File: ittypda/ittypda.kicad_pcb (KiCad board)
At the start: 2 copper layers, 105 x 109.8 mm, 172 parts, among them CN1 S2B-PH-SM4-TB, J1 USB_C_Receptacle_USB2.0_14P, J13 Conn_01x05_Pin, J14 Conn_01x05_Pin, J2 Conn_01x04_Pin, SW1 Switch, SW10 Switch, SW11 Switch, SW12 Switch, SW13 Switch, SW14 Switch, SW15 Switch, SW16 Switch, SW17 Switch, SW18 Switch, SW19 Switch, SW2 Switch, SW20 Switch, SW21 Switch, SW22 Switch, SW23 Switch, SW24 Switch, SW25 SLIDE SWITCH, SW26 Switch, SW27 Switch, SW28 Switch, SW29 Switch, SW3 Switch, SW30 Switch, SW31 Switch, SW32 Switch, SW33 Switch, SW34 Switch, SW36 Switch, SW37 Switch, SW38 Switch, SW39 Switch, SW4 Switch, SW41 Switch, SW42 Switch, SW43 Switch, SW44 Switch, SW45 Switch, SW46 Switch, SW47 Switch, SW48 Switch, SW49 Switch, SW5 Switch, SW50 Switch, SW51 Switch, SW52 Switch, SW53 Switch, SW54 Switch, SW55 Switch, SW56 Switch, SW57 Switch, SW58 Switch, SW59 Switch, SW6 Switch, SW60 Switch, SW61 Switch, SW7 Switch, SW8 Switch, SW9 Switch, U1 TPS63001, U2 BQ24040DSQR, U4 STM32F411RETx, Y1 16Mhz

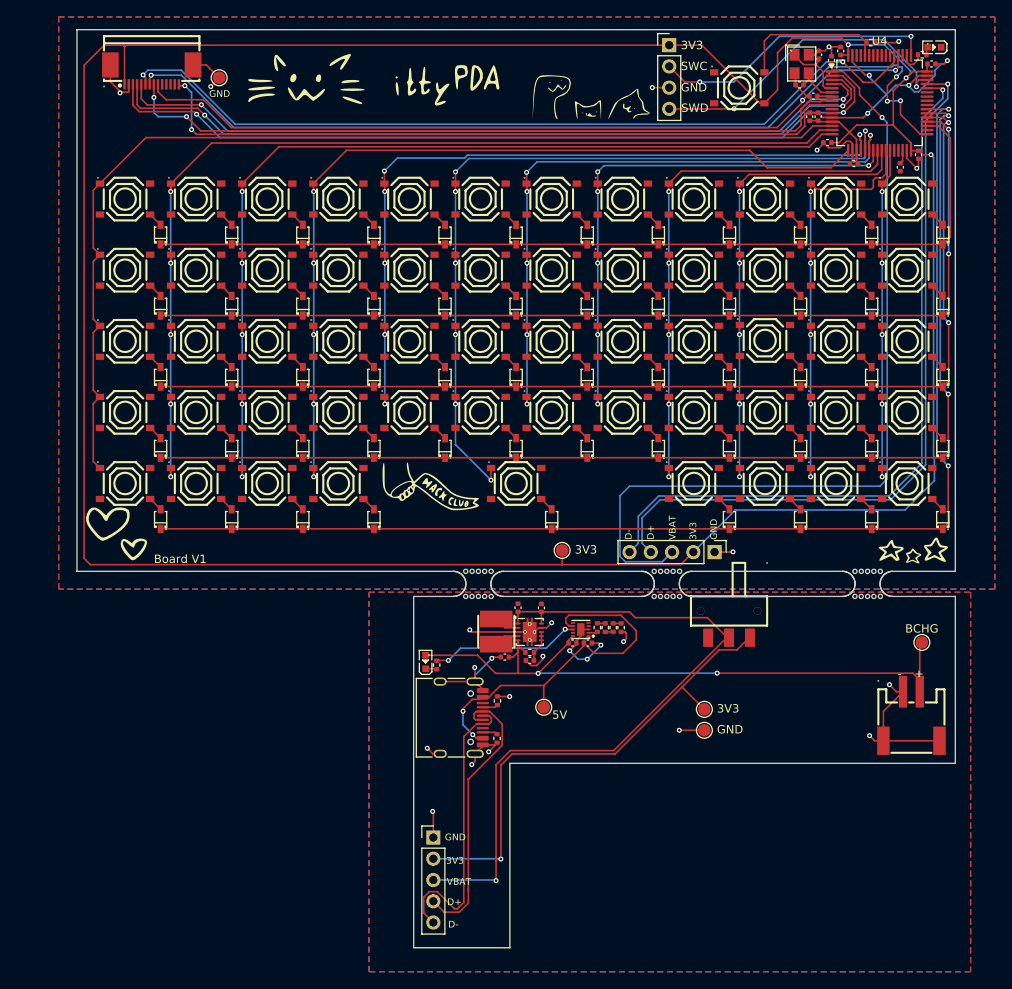
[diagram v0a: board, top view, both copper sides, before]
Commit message: spread out signal lines for better signal integrity
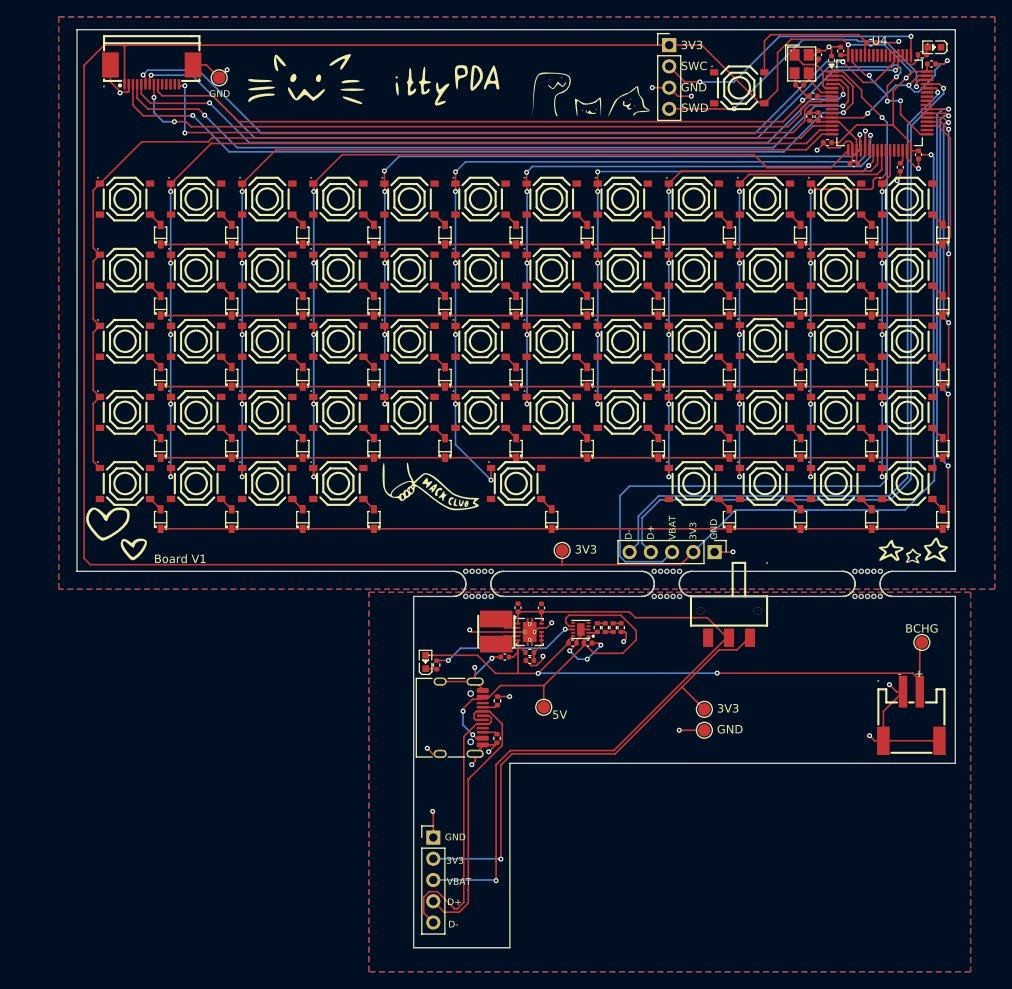
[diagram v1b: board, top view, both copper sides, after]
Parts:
- moved G*** 0.33 mm to (85.5, 38.5)
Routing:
- net GND: track 144.1 -> 148.5 mm, vias 29 -> 31
- net LCD_CS: track 97.1 -> 98.4 mm
- net LED: track 88.0 -> 86.8 mm
- net InD+: track 90.1 -> 89.1 mm
- net MOSI: track 99.9 -> 100.8 mm
- net InD-: track 88.9 -> 88.0 mm
- net SCK: track 108.9 -> 109.6 mm
- net MISO: track 95.7 -> 95.1 mm

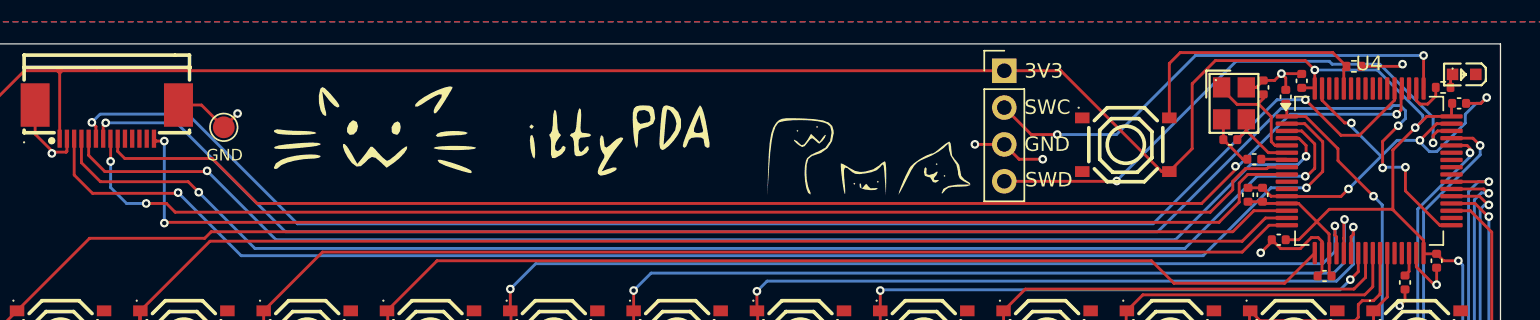
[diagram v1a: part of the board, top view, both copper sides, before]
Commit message: move sck pin and remove sharp turns in MISO and SCK traces
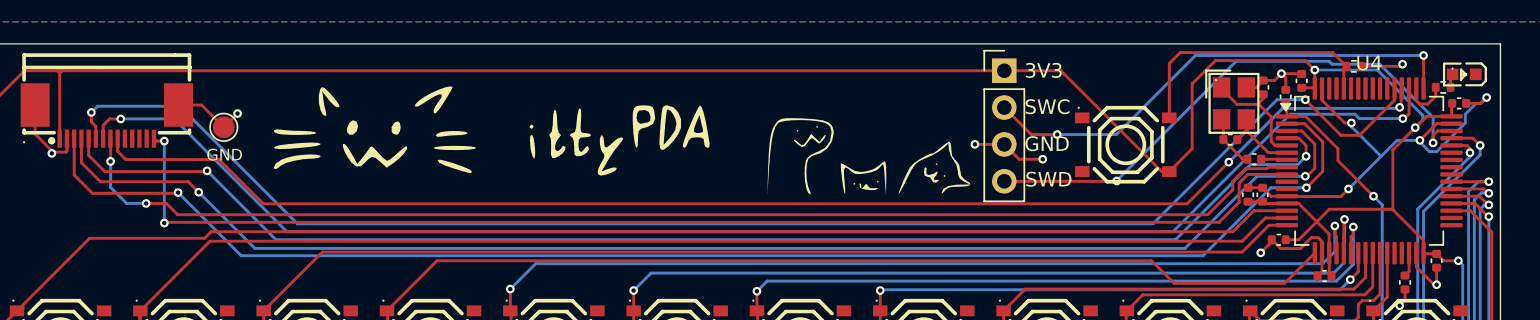
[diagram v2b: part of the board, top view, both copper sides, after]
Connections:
- U4 pad 33: SCK -> unconnected-(U4-PB12-Pad33)
- U4 pad 51: unconnected-(U4-PC10-Pad51) -> SCK
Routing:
- net SCK: track 109.6 -> 99.7 mm, vias 4 -> 2
- net MOSI: track 100.8 -> 101.7 mm
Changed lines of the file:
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@@
 			(layers "F.Cu" "F.Mask" "F.Paste")
 			(roundrect_rratio 0.25)
-			(net "SCK")
+			(net "unconnected-(U4-PB12-Pad33)")
 			(pinfunction "PB12_33")
 			(pintype "bidirectional")
@@
 			(layers "F.Cu" "F.Mask" "F.Paste")
 			(roundrect_rratio 0.25)
-			(net "unconnected-(U4-PC10-Pad51)")
+			(net "SCK")
 			(pinfunction "PC10_51")
 			(pintype "bidirectional")
@@
 	)
 	(segment
-		(start 111.41818 39.35)
-		(end 112.9 39.35)
+		(start 37.05 41.75)
+		(end 37.825 42.525)
 		(width 0.2)
 		(layer "F.Cu")
@@
 	)
 	(segment
-		(start 109 42.35)
-		(end 110.55 40.8)
+		(start 35.65 41.75)
+		(end 37.05 41.75)
 		(width 0.2)
 		(layer "F.Cu")
@@
 	)
 	(segment
-		(start 35.65 41.75)
-		(end 37.05 41.75)
+		(start 110.55 40.21818)
+		(end 111.418181 39.35)
 		(width 0.2)
 		(layer "F.Cu")
@@
 	)
 	(segment
-		(start 37.05 41.75)
-		(end 37.65 42.35)
+		(start 108.825 42.525)
+		(end 110.55 40.8)
 		(width 0.2)
 		(layer "F.Cu")
@@
 	)
 	(segment
-		(start 110.55 40.21818)
-		(end 111.41818 39.35)
+		(start 111.418181 39.35)
+		(end 112.9 39.35)
 		(width 0.2)
 		(layer "F.Cu")
@@
 	)
 	(segment
-		(start 37.65 42.35)
-		(end 109 42.35)
+		(start 112.9 39.35)
+		(end 113 39.25)
 		(width 0.2)
 		(layer "F.Cu")
@@
 	)
 	(segment
-		(start 112.9 39.35)
-		(end 113 39.25)
+		(start 37.825 42.525)
+		(end 108.825 42.525)
 		(width 0.2)
 		(layer "F.Cu")
@@
 	)
 	(segment
-		(start 125.625 43.25)
-		(end 124.81759 43.25)
-		(width 0.2)
-		(layer "F.Cu")
-		(net "SCK")
-	)
-	(segment
-		(start 120.875 39.3)
-		(end 120.875 37.473716)
+		(start 122.269678 35.897894)
+		(end 122.38495 35.897894)
 		(width 0.2)
 		(layer "F.Cu")
@@
 	)
 	(segment
-		(start 122.45 40.88241)
-		(end 122.45 39.25)
+		(start 33.9 35.925)
+		(end 33.120756 35.925)
 		(width 0.2)
 		(layer "F.Cu")
@@
 	)
 	(segment
-		(start 120.875 37.473716)
-		(end 121.955731 36.392985)
+		(start 122.7 35.582844)
+		(end 122.7 33.825)
 		(width 0.2)
 		(layer "F.Cu")
@@
 	)
 	(segment
-		(start 124.81759 43.25)
-		(end 122.45 40.88241)
+		(start 33.120756 35.925)
+		(end 32.6875 36.358256)
 		(width 0.2)
 		(layer "F.Cu")
@@
 	)
 	(segment
-		(start 32.6875 37.285)
-		(end 32.6875 36.364506)
+		(start 122.38495 35.897894)
+		(end 122.7 35.582844)
 		(width 0.2)
 		(layer "F.Cu")
@@
 	)
 	(segment
-		(start 32.6875 36.364506)
-		(end 32.859097 36.192909)
+		(start 32.6875 36.358256)
+		(end 32.6875 37.285)
 		(width 0.2)
 		(layer "F.Cu")
@@
 	)
 	(via
-		(at 121.955731 36.392985)
+		(at 33.9 35.925)
 		(size 0.6)
 		(drill 0.3)
@@
 	)
 	(via
-		(at 32.859097 36.192909)
+		(at 122.269678 35.897894)
 		(size 0.6)
 		(drill 0.3)
@@
 		(net "SCK")
 	)
-	(via
-		(at 122.45 39.25)
-		(size 0.6)
-		(drill 0.3)
-		(layers "F.Cu" "B.Cu")
-		(net "SCK")
-	)
-	(via
-		(at 120.875 39.3)
-		(size 0.6)
-		(drill 0.3)
-		(layers "F.Cu" "B.Cu")
-		(net "SCK")
-	)
-	(segment
-		(start 120.925 39.25)
-		(end 120.875 39.3)
-		(width 0.2)
-		(layer "B.Cu")
-		(net "SCK")
-	)
-	(segment
-		(start 122.45 35.898716)
-		(end 122.45 35.351471)
-		(width 0.2)
-		(layer "B.Cu")
-		(net "SCK")
-	)
 	(segment
-		(start 122.098529 35)
-		(end 121.601471 35)
+		(start 37.575 35.925)
+		(end 45.35 43.7)
 		(width 0.2)
 		(layer "B.Cu")
@@
 	)
 	(segment
-		(start 122.45 35.351471)
-		(end 122.098529 35)
+		(start 106.425 43.7)
+		(end 114.525 35.6)
 		(width 0.2)
 		(layer "B.Cu")
@@
 	)
 	(segment
-		(start 121.601471 35)
-		(end 121.401471 35.2)
+		(start 45.35 43.7)
+		(end 106.425 43.7)
 		(width 0.2)
 		(layer "B.Cu")
@@
 	)
 	(segment
-		(start 121.955731 36.392985)
-		(end 122.45 35.898716)
+		(start 119.271423 35.897894)
+		(end 122.269678 35.897894)
 		(width 0.2)
 		(layer "B.Cu")
@@
 	)
 	(segment
-		(start 45.25 43.7)
-		(end 37.742909 36.192909)
+		(start 114.525 35.6)
+		(end 118.973529 35.6)
 		(width 0.2)
 		(layer "B.Cu")
@@
 	)
 	(segment
-		(start 105.371121 43.7)
-		(end 45.25 43.7)
+		(start 118.973529 35.6)
+		(end 119.271423 35.897894)
 		(width 0.2)
 		(layer "B.Cu")
@@
 	)
 	(segment
-		(start 122.45 39.25)
-		(end 120.925 39.25)
-		(width 0.2)
-		(layer "B.Cu")
-		(net "SCK")
-	)
-	(segment
-		(start 121.401471 35.2)
-		(end 113.871121 35.2)
-		(width 0.2)
-		(layer "B.Cu")
-		(net "SCK")
-	)
-	(segment
-		(start 37.742909 36.192909)
-		(end 32.859097 36.192909)
-		(width 0.2)
-		(layer "B.Cu")
-		(net "SCK")
-	)
-	(segment
-		(start 113.871121 35.2)
-		(end 105.371121 43.7)
+		(start 33.9 35.925)
+		(end 37.575 35.925)
 		(width 0.2)
 		(layer "B.Cu")
@@
 	)
 	(segment
-		(start 108.4 41.75)
-		(end 110.734825 39.415175)
+		(start 40.675 38.725)
+		(end 43.725 41.775)
 		(width 0.2)
 		(layer "F.Cu")
@@
 	)
 	(segment
-		(start 122.15 33.875)
-		(end 122.2 33.825)
+		(start 33.6875 38.16)
+		(end 34.2525 38.725)
 		(width 0.2)
 		(layer "F.Cu")
@@
 	)
 	(segment
-		(start 40.2 38.65)
-		(end 43.3 41.75)
+		(start 34.2525 38.725)
+		(end 40.675 38.725)
 		(width 0.2)
 		(layer "F.Cu")
@@
 	)
 	(segment
-		(start 34.1775 38.65)
-		(end 40.2 38.65)
-		(width 0.2)
-		(layer "F.Cu")
-		(net "MISO")
-	)
-	(segment
-		(start 122.15 35.3)
-		(end 122.15 33.875)
+		(start 122.053202 35.127737)
+		(end 122.15 35.030939)
 		(width 0.2)
 		(layer "F.Cu")
@@
 	)
 	(segment
-		(start 121.85 35.6)
-		(end 122.15 35.3)
+		(start 43.725 41.775)
+		(end 107.4 41.775)
 		(width 0.2)
 		(layer "F.Cu")
@@
 	)
 	(segment
-		(start 43.3 41.75)
-		(end 108.4 41.75)
+		(start 122.15 33.875)
+		(end 122.2 33.825)
 		(width 0.2)
 		(layer "F.Cu")
@@
 	)
 	(segment
-		(start 110.734825 39.415175)
-		(end 110.734825 39.184825)
+		(start 107.4 41.775)
+		(end 110.275 38.9)
 		(width 0.2)
 		(layer "F.Cu")
@@
 	)
 	(segment
-		(start 33.6875 38.16)
-		(end 34.1775 38.65)
+		(start 122.15 35.030939)
+		(end 122.15 33.875)
 		(width 0.2)
 		(layer "F.Cu")
@@
 	)
 	(via
-		(at 121.85 35.6)
+		(at 110.275 38.9)
 		(size 0.6)
 		(drill 0.3)
@@
 	)
 	(via
-		(at 110.734825 39.184825)
+		(at 122.053202 35.127737)
 		(size 0.6)
 		(drill 0.3)
@@
 	)
 	(segment
-		(start 110.915175 39.184825)
-		(end 110.734825 39.184825)
+		(start 113.975 35.2)
+		(end 121.980939 35.2)
 		(width 0.2)
 		(layer "B.Cu")
@@
 	)
 	(segment
-		(start 114.5 35.6)
-		(end 110.915175 39.184825)
+		(start 121.980939 35.2)
+		(end 122.053202 35.127737)
 		(width 0.2)
 		(layer "B.Cu")
@@
 	)
 	(segment
-		(start 121.85 35.6)
-		(end 114.5 35.6)
+		(start 110.275 38.9)
+		(end 113.975 35.2)
 		(width 0.2)
 		(layer "B.Cu")
@@
 	)
 	(segment
-		(start 32.1875 37.285)
-		(end 32.1875 36.447235)
+		(start 31.875 36.134735)
+		(end 31.875 35.475)
 		(width 0.2)
 		(layer "F.Cu")
@@
 	)
 	(segment
+		(start 32.1875 36.447235)
+		(end 31.875 36.134735)
+		(width 0.2)
+		(layer "F.Cu")
+		(net "MOSI")
+	)
+	(segment
 		(start 115.554594 34.6)
 		(end 118.004594 37.05)
@@
 	)
 	(segment
-		(start 32.1875 36.447235)
-		(end 31.904816 36.164551)
+		(start 32.1875 37.285)
+		(end 32.1875 36.447235)
 		(width 0.2)
 		(layer "F.Cu")
@@
 	)
 	(via
-		(at 31.904816 36.164551)
+		(at 31.875 35.475)
 		(size 0.6)
 		(drill 0.3)
@@
 	)
 	(segment
-		(start 115.554594 34.6)
-		(end 113.605247 34.6)
+		(start 37.975 35.05)
+		(end 46.075 43.15)
 		(width 0.2)
 		(layer "B.Cu")
@@
 	)
 	(segment
-		(start 46.075 43.15)
-		(end 38.517909 35.592909)
+		(start 31.875 35.475)
+		(end 32.3 35.05)
 		(width 0.2)
 		(layer "B.Cu")
@@
 	)
 	(segment
-		(start 38.517909 35.592909)
-		(end 32.476458 35.592909)
+		(start 32.3 35.05)
+		(end 37.975 35.05)
 		(width 0.2)
 		(layer "B.Cu")
@@
 	)
 	(segment
-		(start 105.055247 43.15)
-		(end 46.075 43.15)
+		(start 46.075 43.15)
+		(end 105.055247 43.15)
 		(width 0.2)
 		(layer "B.Cu")
@@
 	)
 	(segment
-		(start 113.605247 34.6)
-		(end 105.055247 43.15)
+		(start 105.055247 43.15)
+		(end 113.605247 34.6)
 		(width 0.2)
 		(layer "B.Cu")
@@
 	)
 	(segment
-		(start 32.476458 35.592909)
-		(end 31.904816 36.164551)
+		(start 113.605247 34.6)
+		(end 115.554594 34.6)
 		(width 0.2)
 		(layer "B.Cu")
